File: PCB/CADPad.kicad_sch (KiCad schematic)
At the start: 0 parts

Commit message: pcb
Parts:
- added C1, C10, C2, C3, C4, C5, C6, C8: 1uf, Capacitor_SMD:C_0603_1608Metric, symbol Device:C
- added C11, C12, C7, C9: 100nf, Capacitor_SMD:C_0603_1608Metric, symbol Device:C
- added C13, C14: 4.7uF, Capacitor_SMD:C_0603_1608Metric, symbol Device:C
- added CN1: S2B-PH-SM4-TB, easyeda2kicad:CONN-SMD_P2.00_S2B-PH-SM4-TB-LF-SN, symbol easyeda2kicad:S2B-PH-SM4-TB
- added D1, D10, D11, D12, D13, D14, D15, D16, D17, D18, D19, D2, D20, D21, D22, D23, D24, D25, D26, D27, D28, D29, D3, D30, D4, D5, D6, D7, D8, D9: (no value), Diode_SMD:D_SOD-123, symbol ScottoKeebs:Placeholder_Diode
- added Q1: FS8205A_C2830320, easyeda2kicad:SOT-23-6_L2.9-W1.6-P0.95-LS2.8-BR, symbol easyeda2kicad:FS8205A_C2830320
- added R1, R10, R13, R2, R3, R4, R5, R6, R7, R8, R9: 5.1k, Resistor_SMD:R_0603_1608Metric, symbol Device:R
- added R11: 100, Resistor_SMD:R_0603_1608Metric, symbol Device:R
- added R12, R14, R19: 1k, Resistor_SMD:R_0603_1608Metric, symbol Device:R
- added S1, S10, S11, S12, S13, S14, S15, S16, S17, S18, S19, S2, S20, S21, S22, S23, S24, S25, S26, S27, S3, S4, S5, S6, S7, S8, S9: (no value), Switch_Keyboard_Hotswap_Kailh:SW_Hotswap_Kailh_MX, symbol ScottoKeebs:Placeholder_Keyswitch
- added SW1, SW2: EC11E15244G1, easyeda2kicad:SW-TH_EC11E15244G1, symbol easyeda2kicad:EC11E15244G1
- added U1: Nice_Nano_V2, ScottoKeebs_MCU:Nice_Nano_V2, symbol ScottoKeebs:MCU_Nice_Nano_V2
- added U2: SL2.1S, easyeda2kicad:SSOP-16_L4.6-W2.6-P0.53-LS4.0-BL, symbol easyeda2kicad:SL2.1S
- added U3: DW01A_C351410, easyeda2kicad:SOT-23-6_L2.9-W1.6-P0.95-LS2.8-BL, symbol easyeda2kicad:DW01A_C351410
- added U4: MCP73831T-2ACI/OT, easyeda2kicad:SOT-23-5_L3.0-W1.7-P0.95-LS2.8-BL, symbol easyeda2kicad:MCP73831T-2ACI_OT
- added USB1, USB2, USB3, USB4, USB5: TYPE-C 16PIN 2MD, easyeda2kicad:USB-C-SMD_TYPE-C-6PIN-2MD-073, symbol easyeda2kicad:TYPE-C16PIN2MD
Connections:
- new net: D21.2 (A), S21.2
- new net: D3.2 (A), S3.2
- new net: R14.1, R19.2
- new net: D17.2 (A), S17.2
- new net: D25.2 (A), S25.2
- new net: R9.2, USB5.10 (CC2)
- new net: R5.2, USB3.10 (CC2)
- new net: R6.2, USB3.4 (CC1)
- new net: D5.2 (A), S5.2
- new net: R1.1, USB1.4 (CC1)
- new net: D4.2 (A), S4.2
- new net: C8.1, C9.1, U2.9 (VDD33)
- new net: D9.2 (A), S9.2
- new net: R10.2, USB5.4 (CC1)
- new net: D2.2 (A), S2.2
- new net: Q1.6 (G1), U3.1 (OD)
- new net: R12.2, U3.2 (VM)
- new net: Q1.4 (G2), U3.3 (OC)
- new net: C12.2, R11.1, U3.5 (VCC)
- new net: R7.2, USB4.10 (CC2)
- new net: D10.2 (A), S10.2
- new net: R2.1, USB1.10 (CC2)
- new net: D29.2 (A), S27.2
- new net: D28.2 (A), S26.2
- new net: D23.2 (A), S23.2
- new net: R4.2, USB2.4 (CC1)
- new net: D1.2 (A), S1.2
- new net: D24.2 (A), S24.2
- new net: D22.2 (A), S22.2
- new net: D20.2 (A), S20.2
- new net: D8.2 (A), S8.2
- new net: D15.2 (A), S15.2
- new net: D30.1 (K), U1.24 (B+)
- new net: C10.1, C11.1, U2.10 (VDD18)
- new net: D7.2 (A), S7.2
- new net: R8.2, USB4.4 (CC1)
- new net: D11.2 (A), S11.2
- new net: R14.2, U4.5 (PROG)
- new net: D12.2 (A), S12.2
- new net: D13.2 (A), S13.2
- new net: R3.2, USB2.10 (CC2)
- new net: D14.2 (A), S14.2
- new net: D16.2 (A), S16.2
- new net: D18.2 (A), S18.2
- new net: D6.2 (A), S6.2
- new net: D19.2 (A), S19.2
- new net +3.3V: R13.1, U1.21 (3.3v)
- new net +5V: C1.1, C14.1, C2.1, C3.1, C4.1, C5.1, C6.1, C7.1, R10.1, R3.1, R4.1, R5.1, R6.1, R7.1, R8.1, R9.1, U2.7 (VDD5), U4.4 (VDD), USB1.11 (VBUS), USB1.2 (VBUS), USB2.11 (VBUS), USB2.2 (VBUS), USB3.11 (VBUS), USB3.2 (VBUS), USB4.11 (VBUS), USB4.2 (VBUS), USB5.11 (VBUS), USB5.2 (VBUS)
- new net BATT+: C13.1, D30.2 (A), U4.3 (VBAT)
- new net Batt+: CN1.1, R11.2
- new net Batt-: C12.1, CN1.2, Q1.1 (S1), U3.6 (GND)
- new net Column 1: S1.1, S15.1, S22.1, S26.1, S8.1, U1.2 (0)
- new net Column 2: S16.1, S2.1, S23.1, S27.1, S9.1, U1.1
- new net Column 3: S10.1, S17.1, S24.1, S3.1, U1.5 (2)
- new net Column 4: S11.1, S18.1, S25.1, S4.1, U1.6 (3)
- new net Column 5: S12.1, S19.1, S5.1, SW1.D, U1.7 (4)
- new net Column 6: S13.1, S20.1, S6.1, SW2.D, U1.8 (5)
- new net Column 7: S14.1, S21.1, S7.1, U1.9 (6)
- new net D1/D2: Q1.2 (D1/D2), Q1.5 (D1/D2), R12.1
- new net DN: U2.5 (UDM), USB1.5 (DN2), USB1.7 (DN1)
- new net DN1: U2.3 (DM1), USB2.5 (DN2), USB2.7 (DN1)
- new net DN2: U2.1 (DM2), USB3.5 (DN2), USB3.7 (DN1)
- new net DN3: U2.15 (DM3), USB4.5 (DN2), USB4.7 (DN1)
- new net DN4: U2.13 (DM4), USB5.5 (DN2), USB5.7 (DN1)
- new net DP: U2.6 (UDP), USB1.6 (DP1), USB1.8 (DP2)
- new net DP1: U2.4 (DP1), USB2.6 (DP1), USB2.8 (DP2)
- new net DP2: U2.2 (DP2), USB3.6 (DP1), USB3.8 (DP2)
- new net DP3: U2.16 (DP3), USB4.6 (DP1), USB4.8 (DP2)
- new net DP4: U2.14 (DP4), USB5.6 (DP1), USB5.8 (DP2)
- new net GND: C1.2, C10.2, C11.2, C13.2, C14.2, C2.2, C3.2, C4.2, C5.2, C6.2, C7.2, C8.2, C9.2, CN1.3, CN1.4, Q1.3 (S2), R1.2, R19.1, R2.2, SW1.6, SW1.7, SW1.C, SW2.6, SW2.7, SW2.C, U1.23 (GND), U1.3 (GND), U1.4 (GND), U2.12 (XIN), U2.8 (VSS), U4.2 (VSS), USB1.1 (GND), USB1.12 (GND), USB1.13 (SHELL), USB1.14 (SHELL), USB2.1 (GND), USB2.12 (GND), USB2.13 (SHELL), USB2.14 (SHELL), USB3.1 (GND), USB3.12 (GND), USB3.13 (SHELL), USB3.14 (SHELL), USB4.1 (GND), USB4.12 (GND), USB4.13 (SHELL), USB4.14 (SHELL), USB5.1 (GND), USB5.12 (GND), USB5.13 (SHELL), USB5.14 (SHELL)
- new net Knob_1 A: SW1.A, U1.15 (14)
- new net Knob_1 B: SW1.B, U1.16 (15)
- new net Knob_1 S_Out: D26.2 (A), SW1.E
- new net Knob_2 A: SW2.A, U1.17 (18)
- new net Knob_2 B: SW2.B, U1.18 (19)
- new net Knob_2 S_Out: D27.2 (A), SW2.E
- new net Row 1: D1.1 (K), D2.1 (K), D3.1 (K), D4.1 (K), D5.1 (K), D6.1 (K), D7.1 (K), U1.10 (7)
- new net Row 2: D10.1 (K), D11.1 (K), D12.1 (K), D13.1 (K), D14.1 (K), D8.1 (K), D9.1 (K), U1.11 (8)
- new net Row 3: D15.1 (K), D16.1 (K), D17.1 (K), D18.1 (K), D19.1 (K), D20.1 (K), D21.1 (K), U1.12 (9)
- new net Row 4: D22.1 (K), D23.1 (K), D24.1 (K), D25.1 (K), D26.1 (K), D27.1 (K), U1.13 (10)
- new net Row 5: D28.1 (K), D29.1 (K), U1.14 (16)
- new net STAT: R13.2, U1.19 (20), U4.1 (STAT)
- no-connect marks 0 -> 17

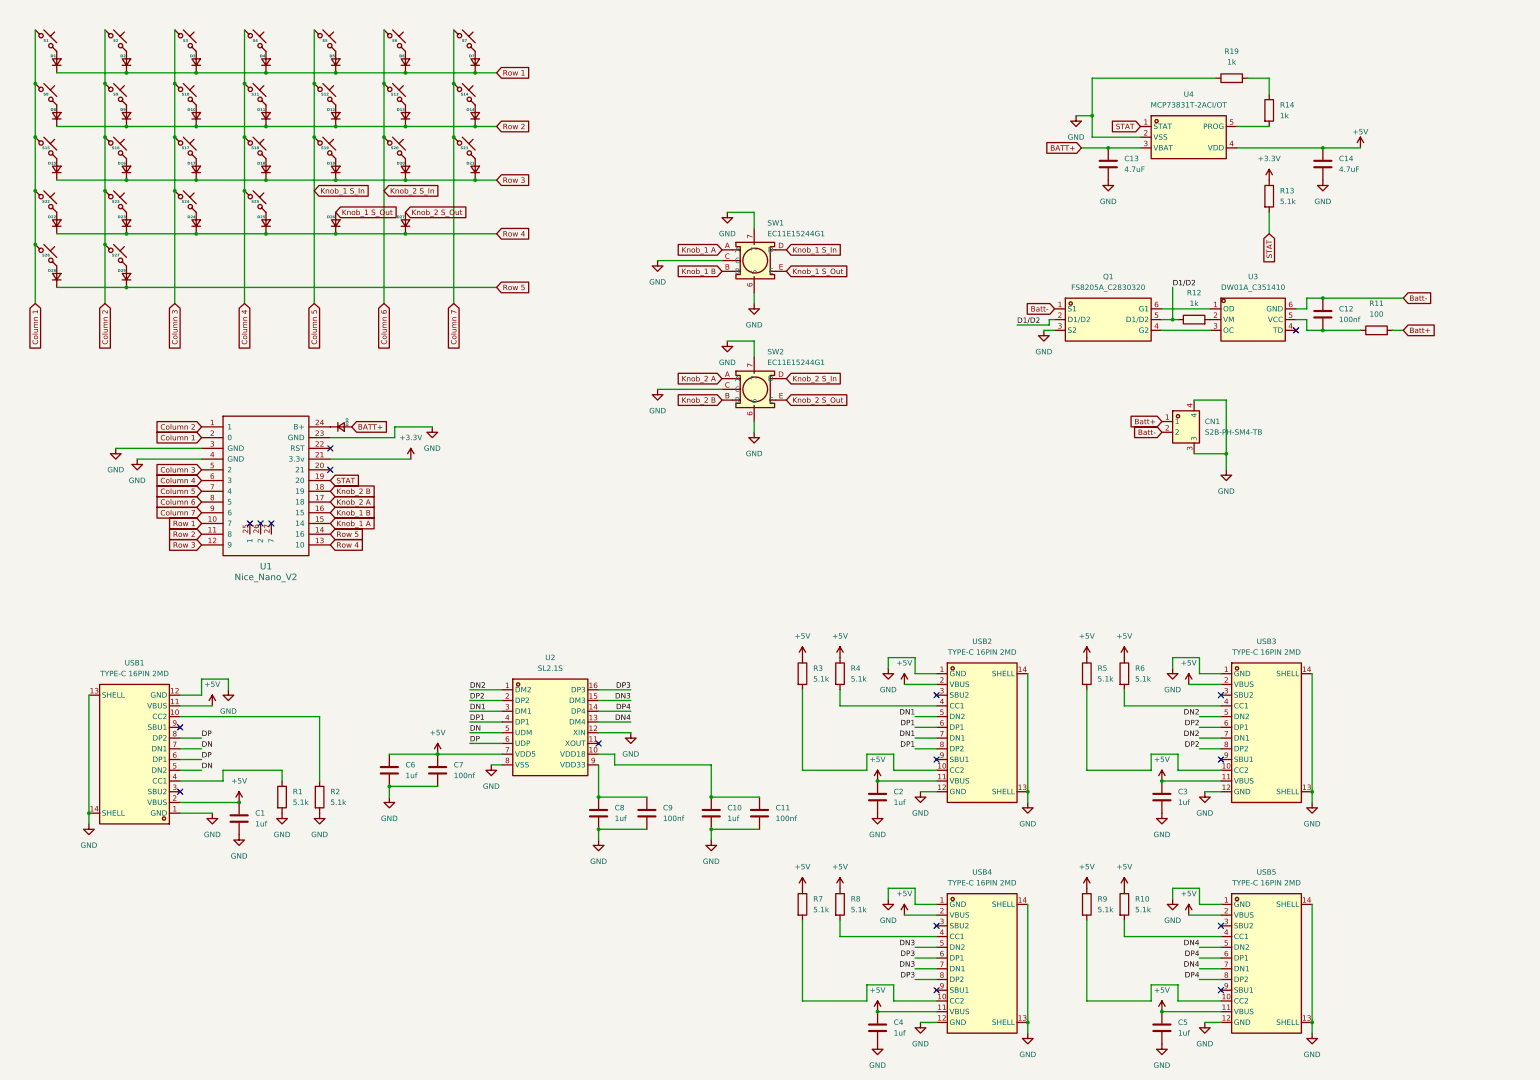
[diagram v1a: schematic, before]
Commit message: assigning LSCS numbers and regenerating PCB-CAD
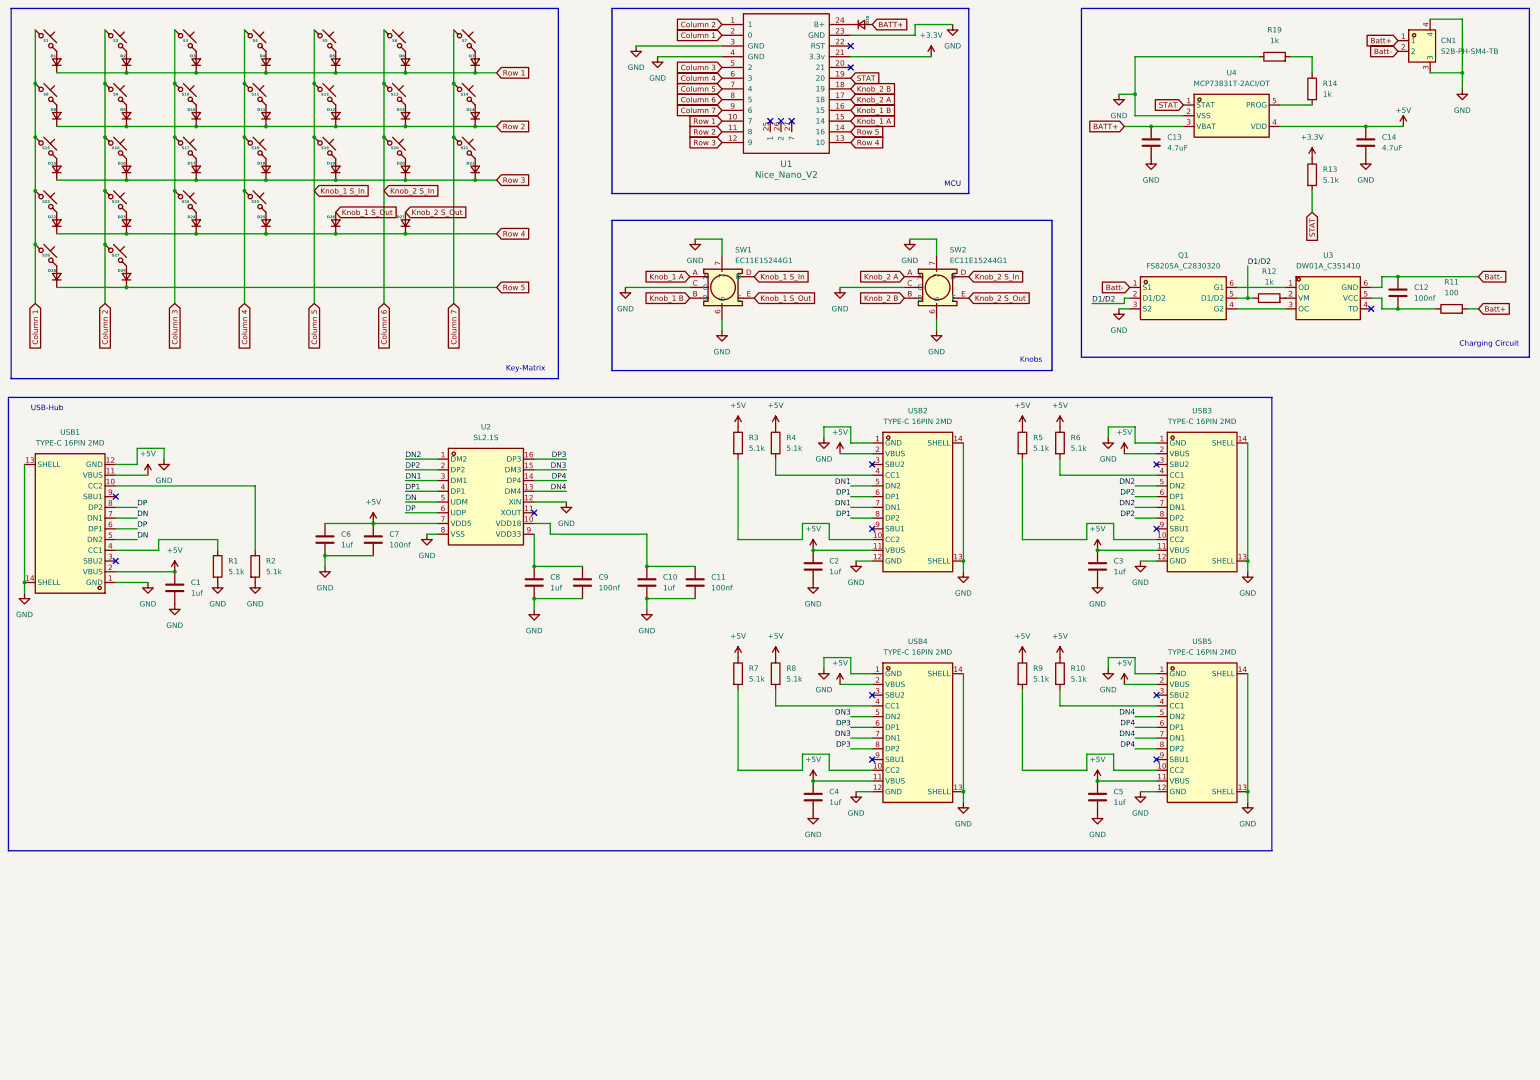
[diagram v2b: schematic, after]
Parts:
- C1, C10, C2, C3, C4, C5, C6, C8: LCSC Part (none) -> C15849
- C11, C12, C7, C9: LCSC Part (none) -> C14663
- D1, D10, D11, D12, D13, D14, D15, D16, D17, D18, D19, D2, D20, D21, D22, D23, D24, D25, D26, D27, D28, D29, D3, D30, D4, D5, D6, D7, D8, D9: LCSC Part (none) -> C81598
- R1, R10, R2, R3, R4, R5, R6, R7, R8, R9: LCSC Part (none) -> C23186
- R11: LCSC Part (none) -> C22775
- R12: LCSC Part (none) -> C21190
- S1, S10, S11, S12, S13, S14, S15, S16, S17, S18, S19, S2, S20, S21, S22, S23, S24, S25, S26, S27, S3, S4, S5, S6, S7, S8, S9: LCSC Part (none) -> C2803348
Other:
- note added: "Charging Circuit"
- note added: "Key-Matrix"
- note added: "Knobs"
- note added: "MCU"
- note added: "USB-Hub"
- moved on the sheet: C1, C10, C11, C12, C13, C14, C2, C3, C4, C5, C6, C7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

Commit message: enhance BOM
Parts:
- SW1, SW2: now left out of the parts list
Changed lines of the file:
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@@
 		(body_style 1)
 		(exclude_from_sim no)
-		(in_bom yes)
+		(in_bom no)
 		(on_board yes)
 		(in_pos_files yes)
@@
 		(body_style 1)
 		(exclude_from_sim no)
-		(in_bom yes)
+		(in_bom no)
 		(on_board yes)
 		(in_pos_files yes)
